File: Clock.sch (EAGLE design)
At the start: 52 parts, among them IC1 A1301UA, U2 3.3V, U3 ATMEGA328

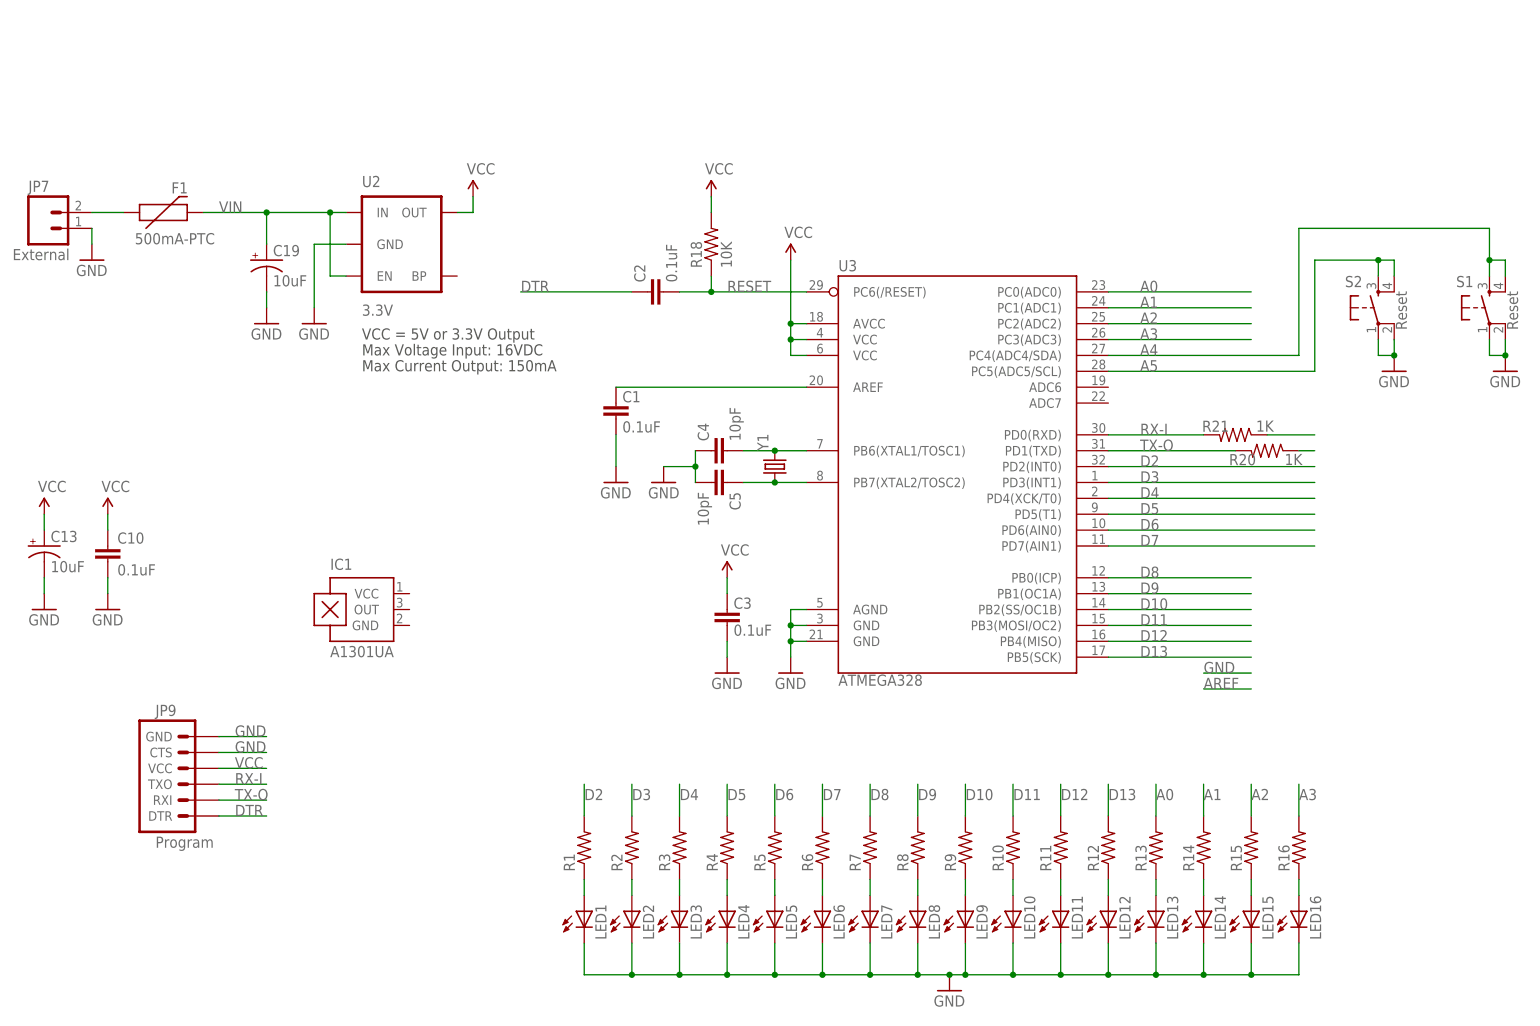
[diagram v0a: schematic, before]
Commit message: Fully routed board
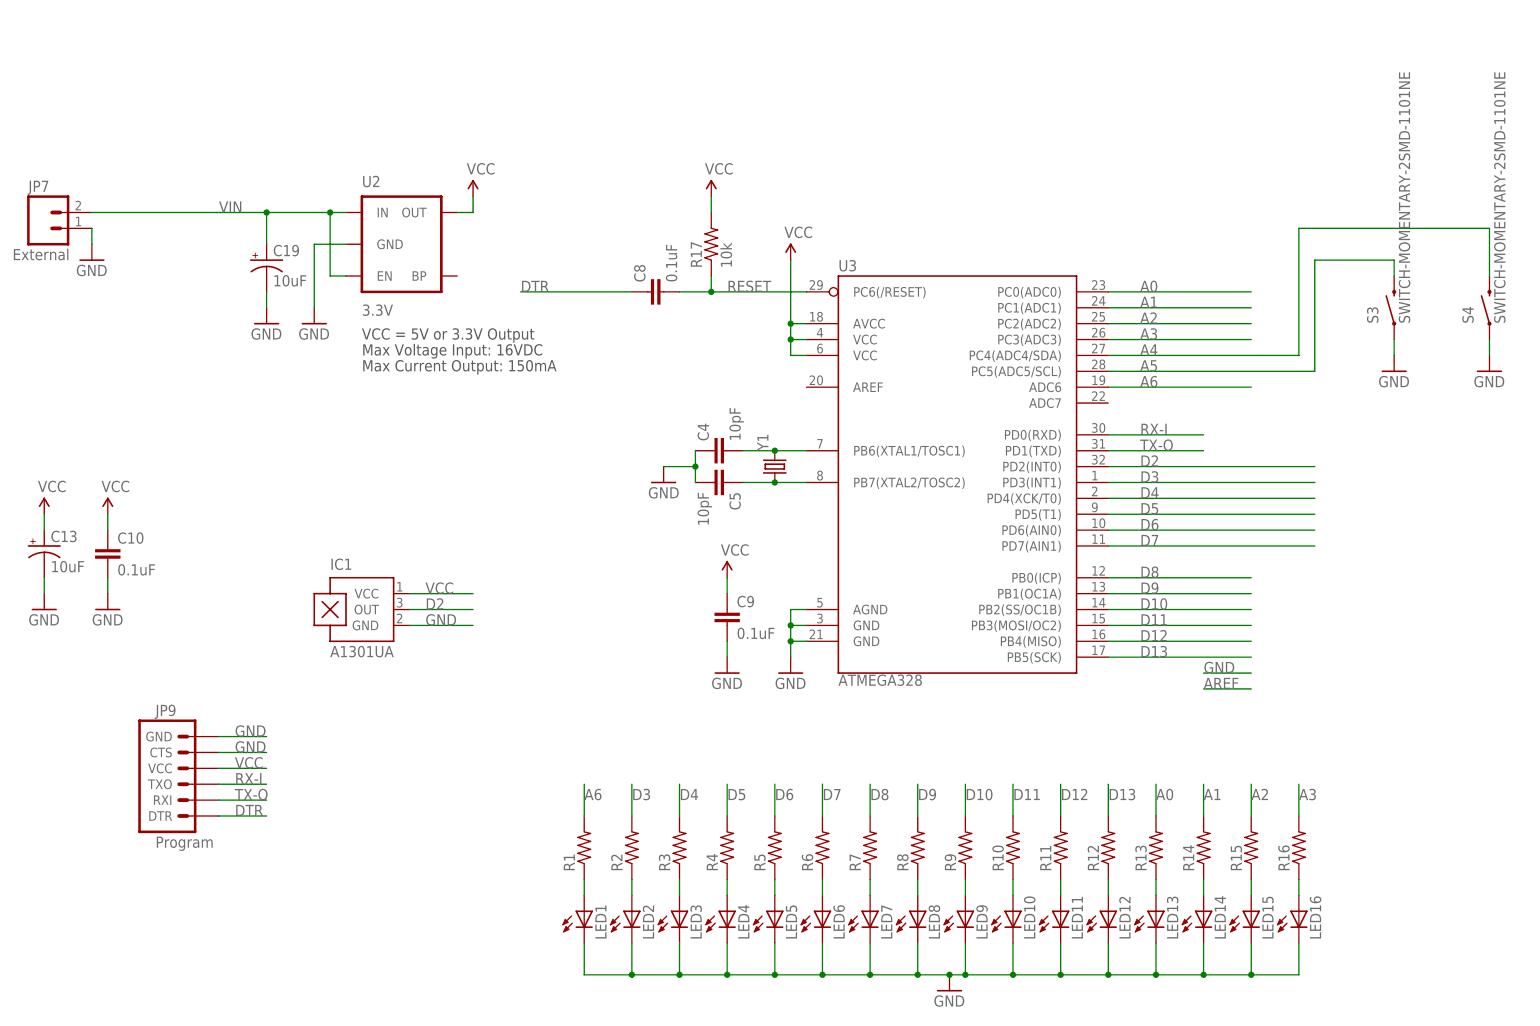
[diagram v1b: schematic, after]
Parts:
- removed C1, C2, C3: 0.1uF, SparkFun:CAP0402-CAP
- removed F1: 500mA-PTC, SparkFun:PTCSMD
- removed R18: 10K, SparkFun:RESISTOR0402-RES
- removed R20, R21: 1K, SparkFun:RESISTOR0402-RES
- removed S1, S2: Reset, SparkFun:TAC_SWITCHSMD
- added C8, C9: 0.1uF, SparkFun-Passives:CAP0603-CAP
- added R17: 10k, SparkFun-Passives:RESISTOR0603-RES
- added S3, S4: SWITCH-MOMENTARY-2SMD-1101NE, SparkFun-Electromechanical:SWITCH-MOMENTARY-2SMD-1101NE
- C10: device SparkFun:CAP0402-CAP -> SparkFun-Passives:CAP0603-CAP
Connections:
- removed net AREF: C1.2, U3.AREF
- removed net N$25: F1.1
- removed net RX-IP: R20.1
- removed net TX-OP: R21.1
- new net A6: R1.2, U3.ADC6
- net A4: now also S4.2; no longer S1.3, S1.4
- net A5: now also S3.2; no longer S2.3, S2.4
- net D2: now also IC1.OUT; no longer R1.2
- net DTR: now also C8.1; no longer C2.1
- net GND: now also C9.2, IC1.GND, S3.1, S4.1; no longer C1.1, C3.1, S1.1, S1.2, S2.1, S2.2
- net RESET: now also C8.2, R17.1; no longer C2.2, R18.1
- net RX-I: no longer R21.2
- net TX-O: no longer R20.2
- net VCC: now also C9.1, IC1.VCC, R17.2; no longer C3.2, R18.2
- net VIN: now also JP7.2; no longer F1.2

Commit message: Board updates for final board fab.
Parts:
- JP7: value External -> Vin
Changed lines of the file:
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@@
 <part name="GND30" library="SparkFun" deviceset="GND" device=""/>
 <part name="GND32" library="SparkFun" deviceset="GND" device=""/>
-<part name="JP7" library="SparkFun" deviceset="M02" device="PTH" value="External"/>
+<part name="JP7" library="SparkFun" deviceset="M02" device="PTH" value="Vin"/>
 <part name="GND11" library="SparkFun" deviceset="GND" device=""/>
 <part name="GND4" library="SparkFun" deviceset="GND" device=""/>
